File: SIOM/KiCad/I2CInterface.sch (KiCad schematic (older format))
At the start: 12 parts, among them Q701 BSS138, Q702 BSS138

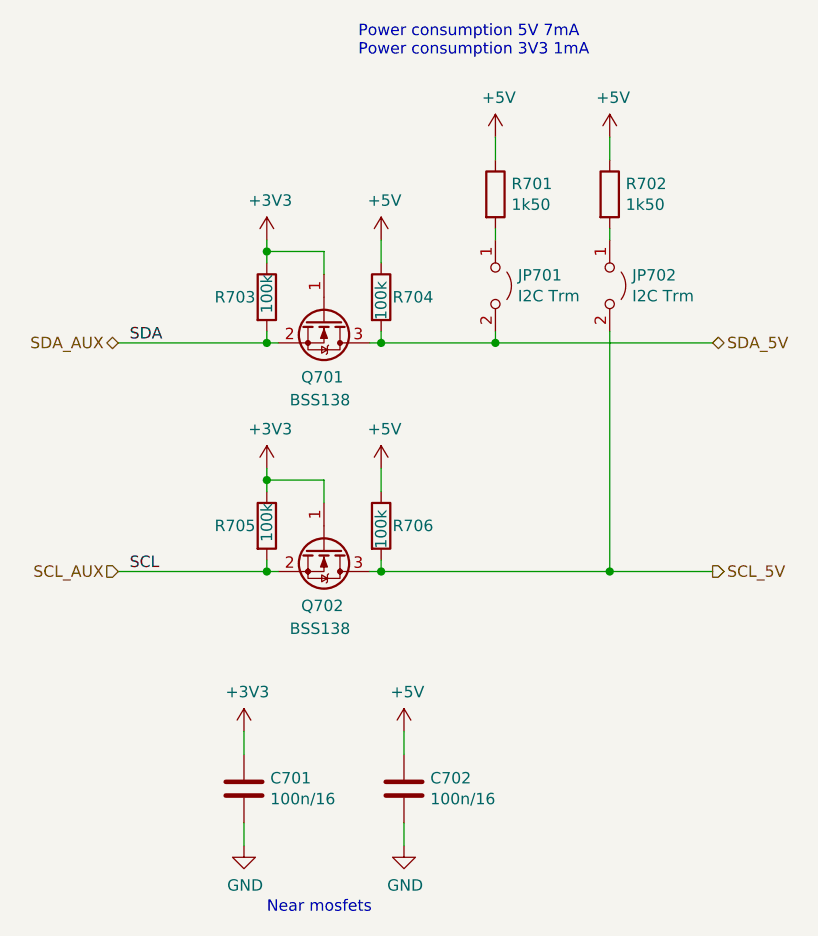
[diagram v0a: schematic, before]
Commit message: KiCad files SIOM_def
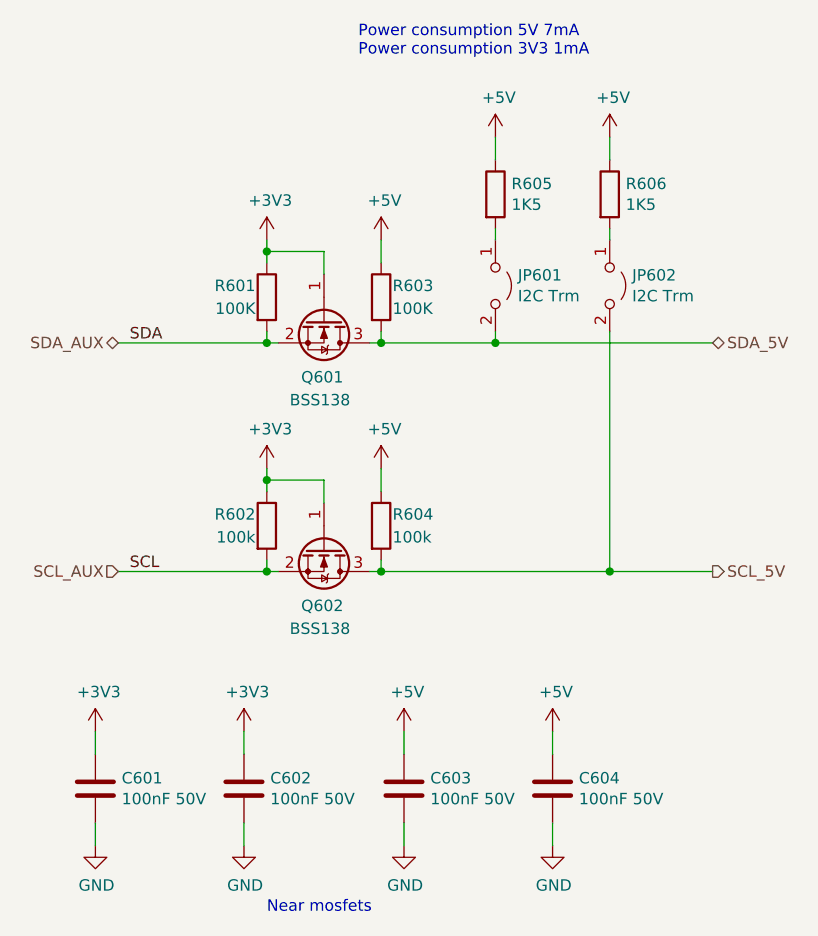
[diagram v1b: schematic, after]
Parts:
- added C601, C604: 100nF 50V, Capacitor_SMD:C_0603_1608Metric, symbol SIOMv01-rescue:C-Device
- C602: renamed from C701; value 100n/16 -> 100nF 50V
- C603: renamed from C702; value 100n/16 -> 100nF 50V
- R601: renamed from R703; value 100k -> 100K
- R603: renamed from R704; value 100k -> 100K
- R605: renamed from R701; value 1k50 -> 1K5
- R606: renamed from R702; value 1k50 -> 1K5
- renumbered JP701 to JP601, JP702 to JP602, Q701 to Q601, Q702 to Q602, R705 to R602, R706 to R604
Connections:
- net +3V3: now also C601.1
- net +5V: now also C604.1
- net GND: now also C601.2, C604.2
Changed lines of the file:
@@
 EESchema Schematic File Version 4
-LIBS:SIOMv01-cache
 EELAYER 30 0
 EELAYER END
 $Descr A4 11693 8268
 encoding utf-8
-Sheet 7 9
+Sheet 6 10
 Title ""
 Date ""
@@
 $EndDescr
 $Comp
-L SIOMv01-rescue:+5V-power #PWR0706
+L SIOMv01-rescue:+5V-power #PWR0608
 U 1 1 5F92B30A
 P 4650 3500
-F 0 "#PWR0706" H 4650 3350 50  0001 C CNN
+F 0 "#PWR0608" H 4650 3350 50  0001 C CNN
 F 1 "+5V" H 4665 3673 50  0000 C CNN
 F 2 "" H 4650 3500 50  0001 C CNN
@@
 $EndComp
 $Comp
-L SIOMv01-rescue:+3V3-power #PWR0705
+L SIOMv01-rescue:+3V3-power #PWR0606
 U 1 1 5F92B310
 P 4150 3500
-F 0 "#PWR0705" H 4150 3350 50  0001 C CNN
+F 0 "#PWR0606" H 4150 3350 50  0001 C CNN
 F 1 "+3V3" H 4165 3673 50  0000 C CNN
 F 2 "" H 4150 3500 50  0001 C CNN
@@
 	4150 3500 4150 3550
 $Comp
-L SIOMv01-rescue:C-Device C701
+L SIOMv01-rescue:C-Device C602
 U 1 1 5F935F05
 P 4050 4900
-F 0 "C701" H 4165 4946 50  0000 L CNN
-F 1 "100n/16" H 4165 4855 50  0000 L CNN
+F 0 "C602" H 4165 4946 50  0000 L CNN
+F 1 "100nF 50V" H 4165 4855 50  0000 L CNN
 F 2 "Capacitor_SMD:C_0603_1608Metric" H 4088 4750 50  0001 C CNN
 F 3 "~" H 4050 4900 50  0001 C CNN
@@
 $EndComp
 $Comp
-L SIOMv01-rescue:GND-power #PWR0709
+L SIOMv01-rescue:GND-power #PWR0604
 U 1 1 5F9432EF
 P 4050 5150
-F 0 "#PWR0709" H 4050 4900 50  0001 C CNN
+F 0 "#PWR0604" H 4050 4900 50  0001 C CNN
 F 1 "GND" H 4055 4977 50  0000 C CNN
 F 2 "" H 4050 5150 50  0001 C CNN
@@
 $EndComp
 $Comp
-L SIOMv01-rescue:+3V3-power #PWR0707
+L SIOMv01-rescue:+3V3-power #PWR0603
 U 1 1 5F94371C
 P 4050 4650
-F 0 "#PWR0707" H 4050 4500 50  0001 C CNN
+F 0 "#PWR0603" H 4050 4500 50  0001 C CNN
 F 1 "+3V3" H 4065 4823 50  0000 C CNN
 F 2 "" H 4050 4650 50  0001 C CNN
@@
 $EndComp
 $Comp
-L SIOMv01-rescue:BSS138-Transistor_FET Q702
+L SIOMv01-rescue:BSS138-Transistor_FET Q602
 U 1 1 5F9A9D35
 P 4400 3850
-F 0 "Q702" V 4650 3750 50  0000 L CNN
+F 0 "Q602" V 4650 3750 50  0000 L CNN
 F 1 "BSS138" V 4750 3700 50  0000 L CNN
 F 2 "Package_TO_SOT_SMD:SOT-23" H 4600 3775 50  0001 L CIN
@@
 $EndComp
 $Comp
-L SIOMv01-rescue:R-Device R705
+L SIOMv01-rescue:R-Device R602
 U 1 1 5F95C195
 P 4150 3750
-F 0 "R705" H 4100 3750 50  0000 R CNN
-F 1 "100k" V 4150 3850 50  0000 R CNN
+F 0 "R602" H 4100 3800 50  0000 R CNN
+F 1 "100k" H 4100 3700 50  0000 R CNN
 F 2 "Resistor_SMD:R_0603_1608Metric" V 4080 3750 50  0001 C CNN
 F 3 "~" H 4150 3750 50  0001 C CNN
@@
 $EndComp
 $Comp
-L SIOMv01-rescue:R-Device R706
+L SIOMv01-rescue:R-Device R604
 U 1 1 5F95CA5A
 P 4650 3750
-F 0 "R706" H 4700 3750 50  0000 L CNN
-F 1 "100k" V 4650 3650 50  0000 L CNN
+F 0 "R604" H 4700 3800 50  0000 L CNN
+F 1 "100k" H 4700 3700 50  0000 L CNN
 F 2 "Resistor_SMD:R_0603_1608Metric" V 4580 3750 50  0001 C CNN
 F 3 "~" H 4650 3750 50  0001 C CNN
@@
 Connection ~ 4650 3950
 $Comp
-L SIOMv01-rescue:+5V-power #PWR0704
+L SIOMv01-rescue:+5V-power #PWR0607
 U 1 1 5F97039E
 P 4650 2500
-F 0 "#PWR0704" H 4650 2350 50  0001 C CNN
+F 0 "#PWR0607" H 4650 2350 50  0001 C CNN
 F 1 "+5V" H 4665 2673 50  0000 C CNN
 F 2 "" H 4650 2500 50  0001 C CNN
@@
 $EndComp
 $Comp
-L SIOMv01-rescue:+3V3-power #PWR0703
+L SIOMv01-rescue:+3V3-power #PWR0605
 U 1 1 5F9703A4
 P 4150 2500
-F 0 "#PWR0703" H 4150 2350 50  0001 C CNN
+F 0 "#PWR0605" H 4150 2350 50  0001 C CNN
 F 1 "+3V3" H 4165 2673 50  0000 C CNN
 F 2 "" H 4150 2500 50  0001 C CNN
@@
 	4150 2500 4150 2550
 $Comp
-L SIOMv01-rescue:BSS138-Transistor_FET Q701
+L SIOMv01-rescue:BSS138-Transistor_FET Q601
 U 1 1 5F9703AC
 P 4400 2850
-F 0 "Q701" V 4650 2750 50  0000 L CNN
+F 0 "Q601" V 4650 2750 50  0000 L CNN
 F 1 "BSS138" V 4750 2700 50  0000 L CNN
 F 2 "Package_TO_SOT_SMD:SOT-23" H 4600 2775 50  0001 L CIN
@@
 $EndComp
 $Comp
-L SIOMv01-rescue:R-Device R703
+L SIOMv01-rescue:R-Device R601
 U 1 1 5F9703B2
 P 4150 2750
-F 0 "R703" H 4100 2750 50  0000 R CNN
-F 1 "100k" V 4150 2850 50  0000 R CNN
+F 0 "R601" H 4100 2800 50  0000 R CNN
+F 1 "100K" H 4100 2700 50  0000 R CNN
 F 2 "Resistor_SMD:R_0603_1608Metric" V 4080 2750 50  0001 C CNN
 F 3 "~" H 4150 2750 50  0001 C CNN
@@
 $EndComp
 $Comp
-L SIOMv01-rescue:R-Device R704
+L SIOMv01-rescue:R-Device R603
 U 1 1 5F9703B8
 P 4650 2750
-F 0 "R704" H 4700 2750 50  0000 L CNN
-F 1 "100k" V 4650 2650 50  0000 L CNN
+F 0 "R603" H 4700 2800 50  0000 L CNN
+F 1 "100K" H 4700 2700 50  0000 L CNN
 F 2 "Resistor_SMD:R_0603_1608Metric" V 4580 2750 50  0001 C CNN
 F 3 "~" H 4650 2750 50  0001 C CNN
@@
 Connection ~ 4650 2950
 $Comp
-L SIOMv01-rescue:C-Device C702
+L SIOMv01-rescue:C-Device C603
 U 1 1 5F9A398F
 P 4750 4900
-F 0 "C702" H 4865 4946 50  0000 L CNN
-F 1 "100n/16" H 4865 4855 50  0000 L CNN
+F 0 "C603" H 4865 4946 50  0000 L CNN
+F 1 "100nF 50V" H 4865 4855 50  0000 L CNN
 F 2 "Capacitor_SMD:C_0603_1608Metric" H 4788 4750 50  0001 C CNN
 F 3 "~" H 4750 4900 50  0001 C CNN
@@
 $EndComp
 $Comp
-L SIOMv01-rescue:GND-power #PWR0710
+L SIOMv01-rescue:GND-power #PWR0610
 U 1 1 5F9A39A7
 P 4750 5150
-F 0 "#PWR0710" H 4750 4900 50  0001 C CNN
+F 0 "#PWR0610" H 4750 4900 50  0001 C CNN
 F 1 "GND" H 4755 4977 50  0000 C CNN
 F 2 "" H 4750 5150 50  0001 C CNN
@@
 $EndComp
 $Comp
-L SIOMv01-rescue:+5V-power #PWR0708
+L SIOMv01-rescue:+5V-power #PWR0609
 U 1 1 5F9A4B24
 P 4750 4650
-F 0 "#PWR0708" H 4750 4500 50  0001 C CNN
+F 0 "#PWR0609" H 4750 4500 50  0001 C CNN
 F 1 "+5V" H 4765 4823 50  0000 C CNN
 F 2 "" H 4750 4650 50  0001 C CNN
@@
 Near mosfets
 $Comp
-L SIOMv01-rescue:Jumper_2_Open-Jumper JP701
+L SIOMv01-rescue:Jumper_2_Open-Jumper JP601
 U 1 1 5F984652
 P 5150 2700
-F 0 "JP701" V 5104 2798 50  0000 L CNN
+F 0 "JP601" V 5104 2798 50  0000 L CNN
 F 1 "I2C Trm" V 5195 2798 50  0000 L CNN
 F 2 "Connector_PinHeader_2.54mm:PinHeader_1x02_P2.54mm_Vertical" H 5150 2700 50  0001 C CNN
@@
 $EndComp
 $Comp
-L SIOMv01-rescue:Jumper_2_Open-Jumper JP702
+L SIOMv01-rescue:Jumper_2_Open-Jumper JP602
 U 1 1 5F98F58F
 P 5650 2700
-F 0 "JP702" V 5604 2798 50  0000 L CNN
+F 0 "JP602" V 5604 2798 50  0000 L CNN
 F 1 "I2C Trm" V 5695 2798 50  0000 L CNN
 F 2 "Connector_PinHeader_2.54mm:PinHeader_1x02_P2.54mm_Vertical" H 5650 2700 50  0001 C CNN
@@
 $EndComp
 $Comp
-L SIOMv01-rescue:+5V-power #PWR0701
+L SIOMv01-rescue:+5V-power #PWR0611
 U 1 1 5F9920CF
 P 5150 2050
-F 0 "#PWR0701" H 5150 1900 50  0001 C CNN
+F 0 "#PWR0611" H 5150 1900 50  0001 C CNN
 F 1 "+5V" H 5165 2223 50  0000 C CNN
 F 2 "" H 5150 2050 50  0001 C CNN
@@
 	5150 2050 5150 2150
 $Comp
-L SIOMv01-rescue:R-Device R701
+L SIOMv01-rescue:R-Device R605
 U 1 1 5F9920D6
 P 5150 2300
-F 0 "R701" H 5220 2346 50  0000 L CNN
-F 1 "1k50" H 5220 2255 50  0000 L CNN
+F 0 "R605" H 5220 2346 50  0000 L CNN
+F 1 "1K5" H 5220 2255 50  0000 L CNN
 F 2 "Resistor_SMD:R_0603_1608Metric" V 5080 2300 50  0001 C CNN
 F 3 "~" H 5150 2300 50  0001 C CNN
@@
 $EndComp
 $Comp
-L SIOMv01-rescue:+5V-power #PWR0702
+L SIOMv01-rescue:+5V-power #PWR0614
 U 1 1 5F992D19
 P 5650 2050
-F 0 "#PWR0702" H 5650 1900 50  0001 C CNN
+F 0 "#PWR0614" H 5650 1900 50  0001 C CNN
 F 1 "+5V" H 5665 2223 50  0000 C CNN
 F 2 "" H 5650 2050 50  0001 C CNN
@@
 	5650 2050 5650 2150
 $Comp
-L SIOMv01-rescue:R-Device R702
+L SIOMv01-rescue:R-Device R606
 U 1 1 5F992D20
 P 5650 2300
-F 0 "R702" H 5720 2346 50  0000 L CNN
-F 1 "1k50" H 5720 2255 50  0000 L CNN
+F 0 "R606" H 5720 2346 50  0000 L CNN
+F 1 "1K5" H 5720 2255 50  0000 L CNN
 F 2 "Resistor_SMD:R_0603_1608Metric" V 5580 2300 50  0001 C CNN
 F 3 "~" H 5650 2300 50  0001 C CNN
@@
 Text HLabel 3500 2950 0    50   BiDi ~ 0
 SDA_AUX
+$Comp
+L SIOMv01-rescue:C-Device C601
+U 1 1 60899804
+P 3400 4900
+F 0 "C601" H 3515 4946 50  0000 L CNN
+F 1 "100nF 50V" H 3515 4855 50  0000 L CNN
+F 2 "Capacitor_SMD:C_0603_1608Metric" H 3438 4750 50  0001 C CNN
+F 3 "~" H 3400 4900 50  0001 C CNN
+	1    3400 4900
+	1    0    0    -1
+$EndComp
+$Comp
+L SIOMv01-rescue:C-Device C604
+U 1 1 60899F68
+P 5400 4900
+F 0 "C604" H 5515 4946 50  0000 L CNN
+F 1 "100nF 50V" H 5515 4855 50  0000 L CNN
+F 2 "Capacitor_SMD:C_0603_1608Metric" H 5438 4750 50  0001 C CNN
+F 3 "~" H 5400 4900 50  0001 C CNN
+	1    5400 4900
+	1    0    0    -1
+$EndComp
+$Comp
+L SIOMv01-rescue:GND-power #PWR0613
+U 1 1 6089A1FD
+P 5400 5150
+F 0 "#PWR0613" H 5400 4900 50  0001 C CNN
+F 1 "GND" H 5405 4977 50  0000 C CNN
+F 2 "" H 5400 5150 50  0001 C CNN
+F 3 "" H 5400 5150 50  0001 C CNN
+	1    5400 5150
+	1    0    0    -1
+$EndComp
+$Comp
+L SIOMv01-rescue:+5V-power #PWR0612
+U 1 1 6089A569
+P 5400 4650
+F 0 "#PWR0612" H 5400 4500 50  0001 C CNN
+F 1 "+5V" H 5415 4823 50  0000 C CNN
+F 2 "" H 5400 4650 50  0001 C CNN
+F 3 "" H 5400 4650 50  0001 C CNN
+	1    5400 4650
+	1    0    0    -1
+$EndComp
+$Comp
+L SIOMv01-rescue:+3V3-power #PWR0601
+U 1 1 6089A981
+P 3400 4650
+F 0 "#PWR0601" H 3400 4500 50  0001 C CNN
+F 1 "+3V3" H 3415 4823 50  0000 C CNN
+F 2 "" H 3400 4650 50  0001 C CNN
+F 3 "" H 3400 4650 50  0001 C CNN
+	1    3400 4650
+	1    0    0    -1
+$EndComp
+$Comp
+L SIOMv01-rescue:GND-power #PWR0602
+U 1 1 6089AD15
+P 3400 5150
+F 0 "#PWR0602" H 3400 4900 50  0001 C CNN
+F 1 "GND" H 3405 4977 50  0000 C CNN
+F 2 "" H 3400 5150 50  0001 C CNN
+F 3 "" H 3400 5150 50  0001 C CNN
+	1    3400 5150
+	1    0    0    -1
+$EndComp
+Wire Wire Line
+	3400 5150 3400 5050
+Wire Wire Line
+	3400 4650 3400 4750
+Wire Wire Line
+	5400 4650 5400 4750
+Wire Wire Line
+	5400 5050 5400 5150
 $EndSCHEMATC
